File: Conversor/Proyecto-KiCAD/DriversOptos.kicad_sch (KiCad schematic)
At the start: 22 parts, among them U12 ACPL-P480, U2 ACPL-P480, U3 ACPL-P480, U4 ACPL-P480, U5 2ED21834-S06J, U6 2ED21834-S06J

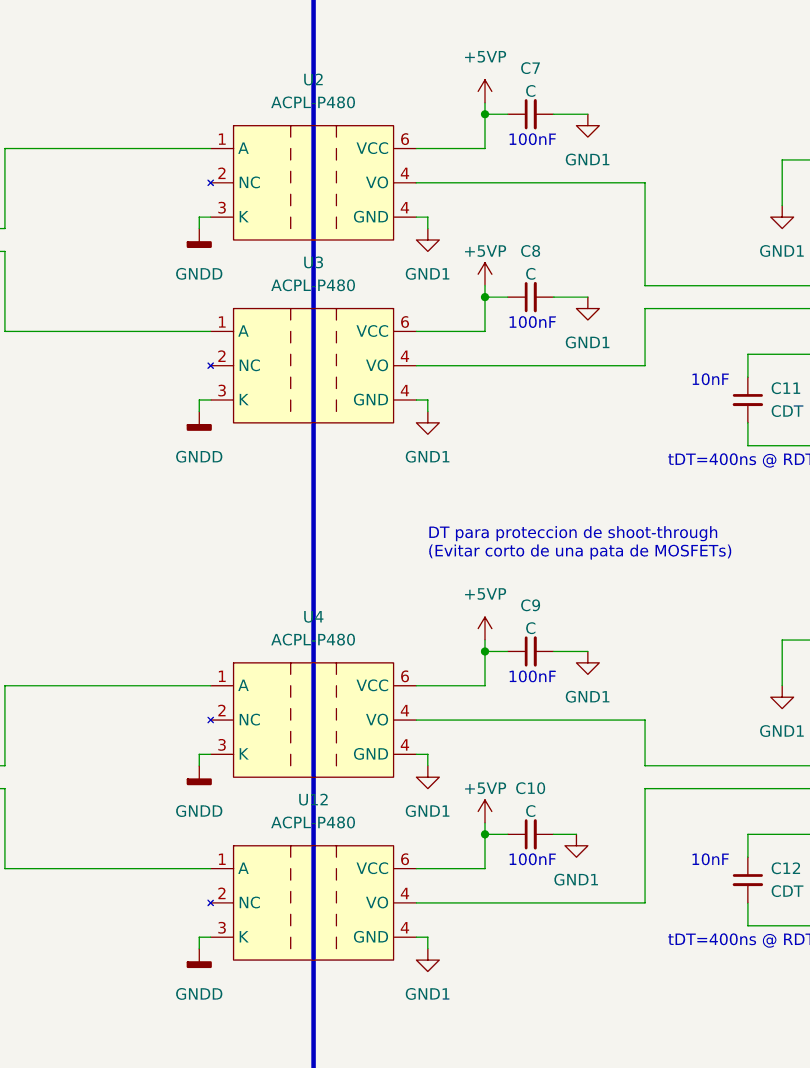
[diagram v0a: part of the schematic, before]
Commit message: Reempezar el ordenado de componentes del PCB
- Intentar copiar mas a la placa adaptadora en la parte del DSP (digital)
  - Algunas cosas (como los headers y la parte de USB) se movieron para hacer entrar mejor las cosas
- Layout bastante completo
- Agregados algunos modelos 3D faltantes
Por hacer:
  - Mover y reorganizar la parte del LM5056, porque tiene una pata que va al secundario, y ahora esta muy lejos del area de GND2
  - Ver como reorganizar un poco para que no queden esquinas vacias
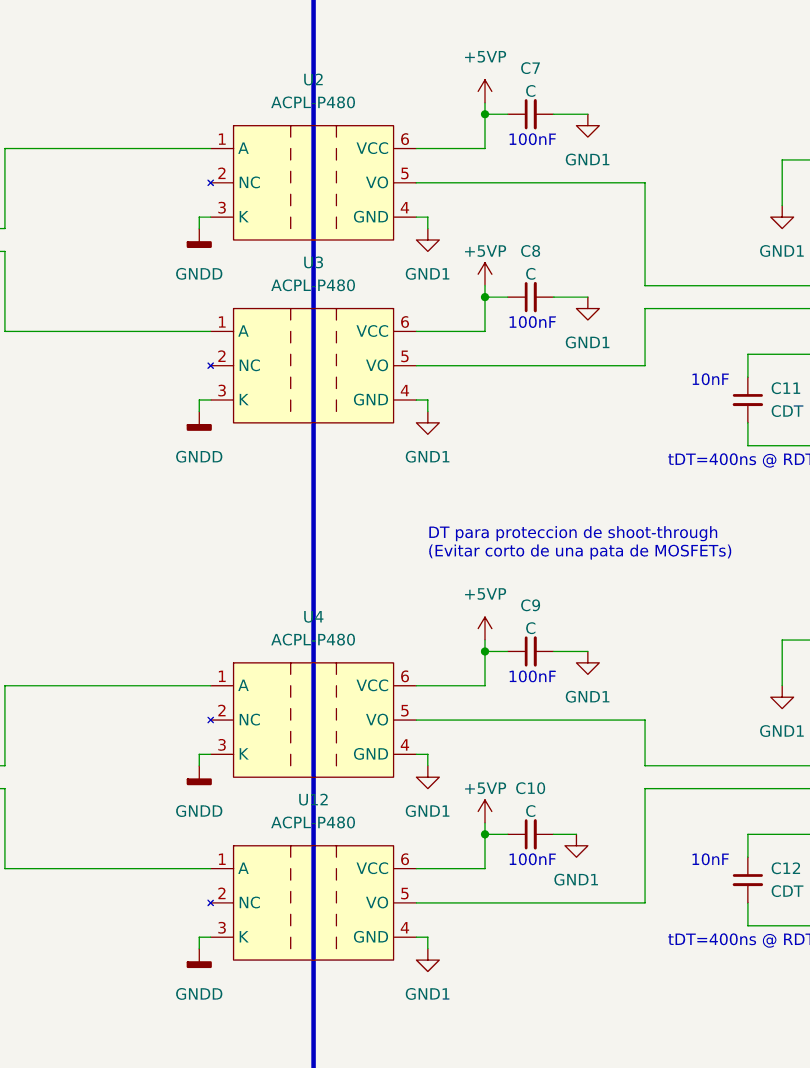
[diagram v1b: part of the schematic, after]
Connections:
- net at U5.1 (HIN): now also U2.5 (VO); no longer U2.4 (VO)
- net at U6.2 (/LIN): now also U12.5 (VO); no longer U12.4 (VO)
- net at U6.1 (HIN): now also U4.5 (VO); no longer U4.4 (VO)
- net at U5.2 (/LIN): now also U3.5 (VO); no longer U3.4 (VO)
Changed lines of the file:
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@@
     (pin "3")
     (pin "4")
-    (pin "4")
+    (pin "5")
     (pin "6")
   )
@@
     (pin "2")
   )
-  (symbol (lib_id "Componentes proyecto:ACPL-P480") (at 125.73 134.62 0) (unit 1)
+  (symbol (lib_name "ACPL-P480_2") (lib_id "Componentes proyecto:ACPL-P480") (at 125.73 134.62 0) (unit 1)
     (in_bom yes) (on_board yes) (fields_autoplaced)
     (property "Reference" "U12" (id 0) (at 125.73 123.19 0))
@@
     (pin "3")
     (pin "4")
-    (pin "4")
+    (pin "5")
     (pin "6")
   )
@@
     (pin "1")
   )
-  (symbol (lib_id "Componentes proyecto:ACPL-P480") (at 125.73 74.93 0) (unit 1)
+  (symbol (lib_name "ACPL-P480_3") (lib_id "Componentes proyecto:ACPL-P480") (at 125.73 74.93 0) (unit 1)
     (in_bom yes) (on_board yes) (fields_autoplaced)
     (property "Reference" "U3" (id 0) (at 125.73 63.5 0))
@@
     (pin "3")
     (pin "4")
-    (pin "4")
+    (pin "5")
     (pin "6")
   )
@@
     (pin "1")
   )
-  (symbol (lib_id "Componentes proyecto:ACPL-P480") (at 125.73 114.3 0) (unit 1)
+  (symbol (lib_name "ACPL-P480_1") (lib_id "Componentes proyecto:ACPL-P480") (at 125.73 114.3 0) (unit 1)
     (in_bom yes) (on_board yes) (fields_autoplaced)
     (property "Reference" "U4" (id 0) (at 125.73 102.87 0))
@@
     (pin "3")
     (pin "4")
-    (pin "4")
+    (pin "5")
     (pin "6")
   )

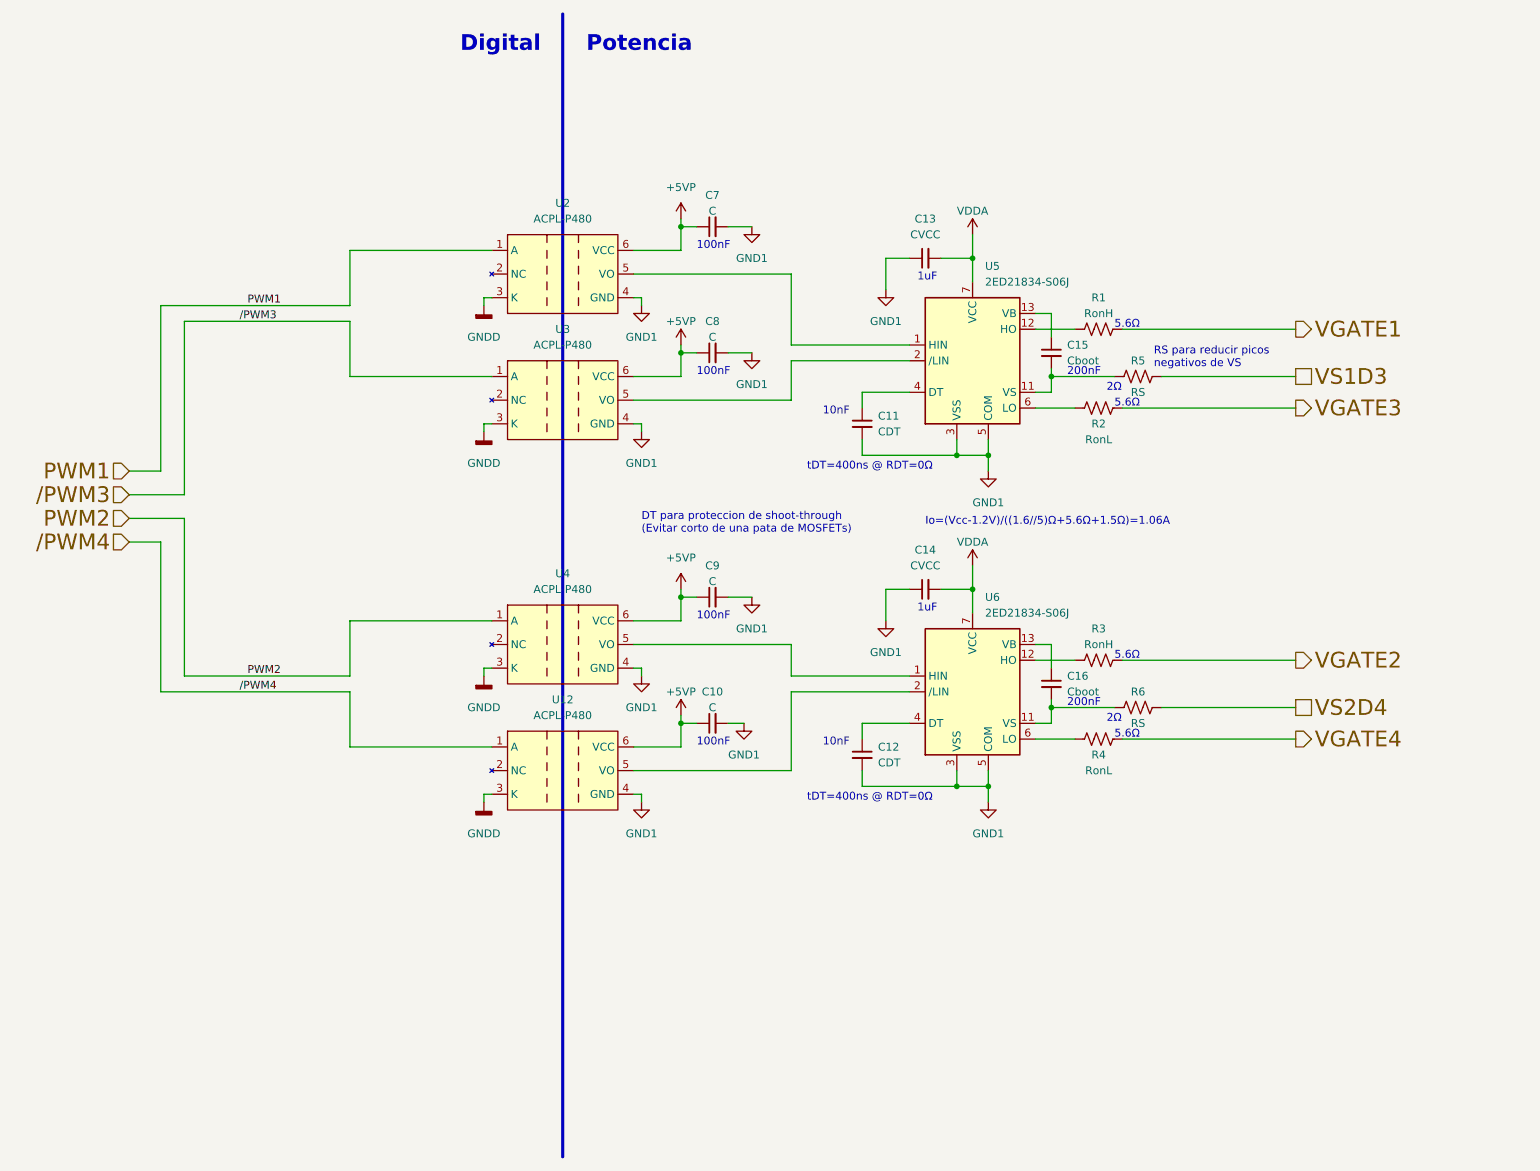
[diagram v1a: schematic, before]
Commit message: Agregar el selector de alim. de 12V y seguir emprolijando la placa
- Agregar modelos de los switches
- Agregar algunos test points
Por hacer:
  - Todo lo de los dos anteriores commits
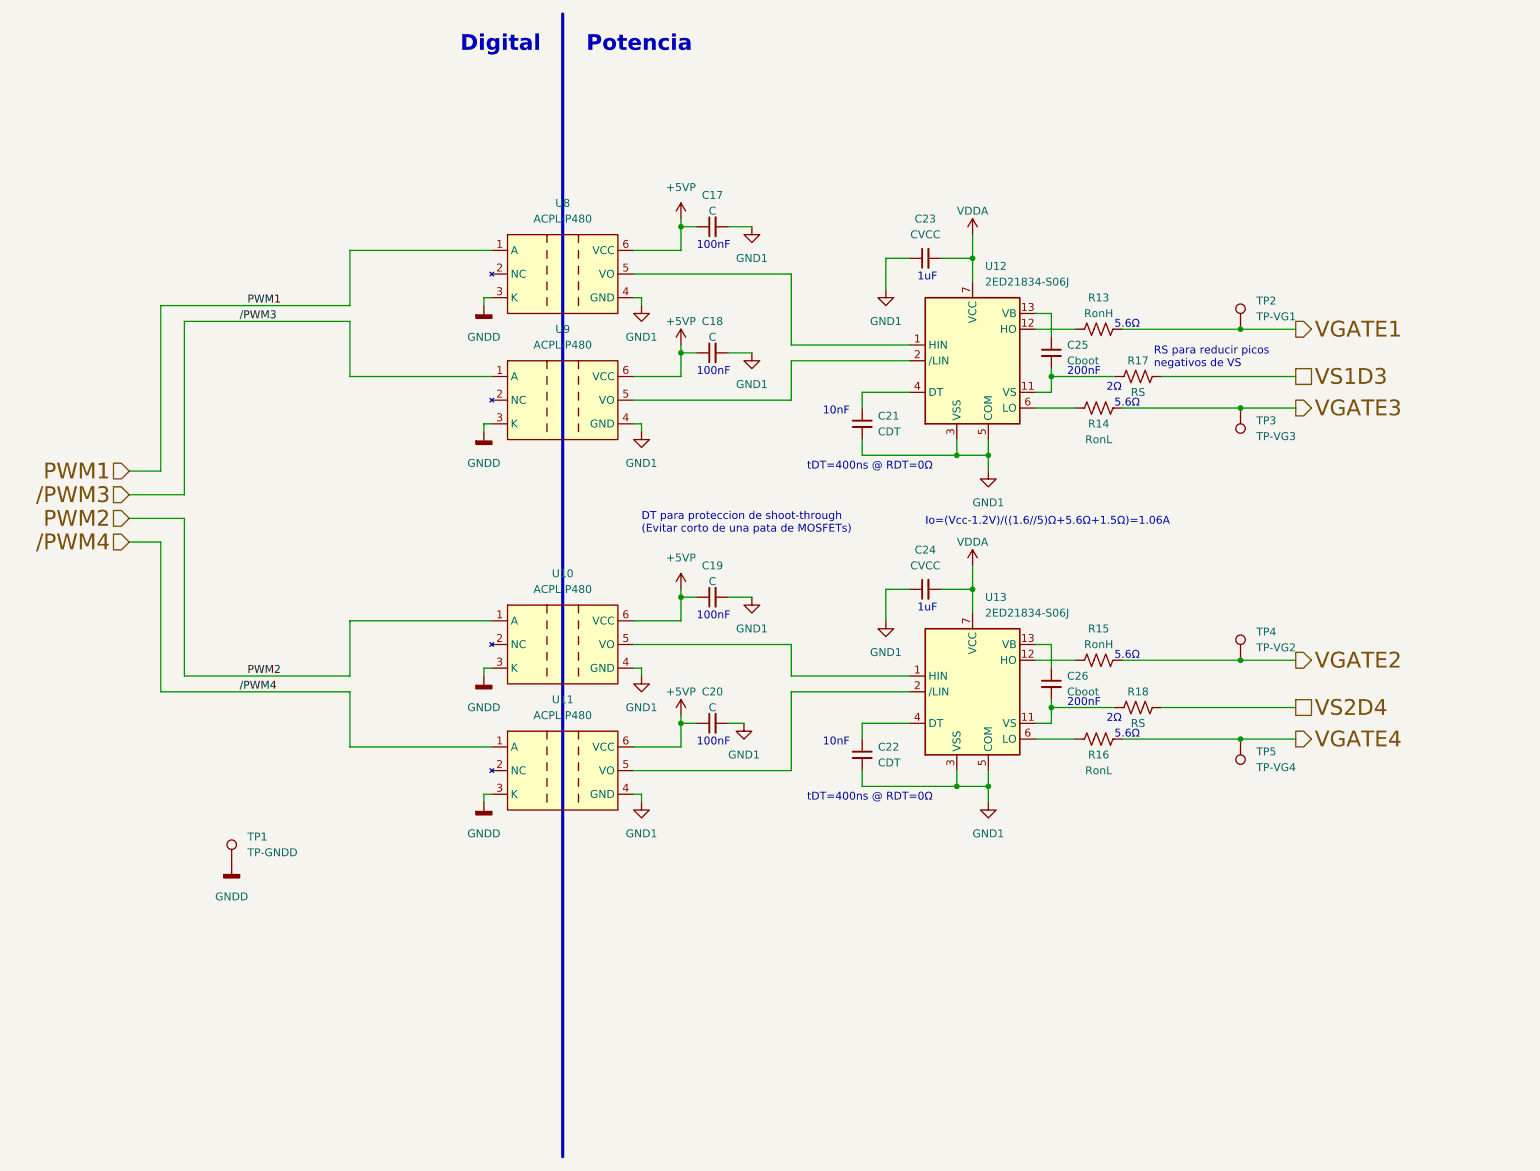
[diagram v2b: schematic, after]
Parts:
- added TP1: TP-GNDD, TestPoint:TestPoint_THTPad_2.0x2.0mm_Drill1.0mm, symbol Connector:TestPoint
- added TP2: TP-VG1, TestPoint:TestPoint_THTPad_2.0x2.0mm_Drill1.0mm, symbol Connector:TestPoint
- added TP3: TP-VG3, TestPoint:TestPoint_THTPad_2.0x2.0mm_Drill1.0mm, symbol Connector:TestPoint
- added TP4: TP-VG2, TestPoint:TestPoint_THTPad_2.0x2.0mm_Drill1.0mm, symbol Connector:TestPoint
- added TP5: TP-VG4, TestPoint:TestPoint_THTPad_2.0x2.0mm_Drill1.0mm, symbol Connector:TestPoint
- renumbered C7 to C17, C8 to C18, C9 to C19, C10 to C20, C11 to C21, C12 to C22, C13 to C23, C14 to C24, C15 to C25, C16 to C26, R1 to R13, R2 to R14, R3 to R15, R4 to R16, R5 to R17, R6 to R18, U4 to U10, U12 to U11, U5 to U12, U6 to U13, U2 to U8, U3 to U9
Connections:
- net GNDD: now also TP1.1
- net VGATE1: now also TP2.1
- net VGATE2: now also TP4.1
- net VGATE3: now also TP3.1
- net VGATE4: now also TP5.1
